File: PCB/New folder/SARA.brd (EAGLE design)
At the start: 76.2 x 76.2 mm, 46 parts, among them U1 MAX9110EKA+T, U2 MAX9110EKA+T, U3 MAX9111EKA+T, U4 MAX9111EKA+T, U5 R-78B3.3-2.0, U6 R-78B3.3-2.0

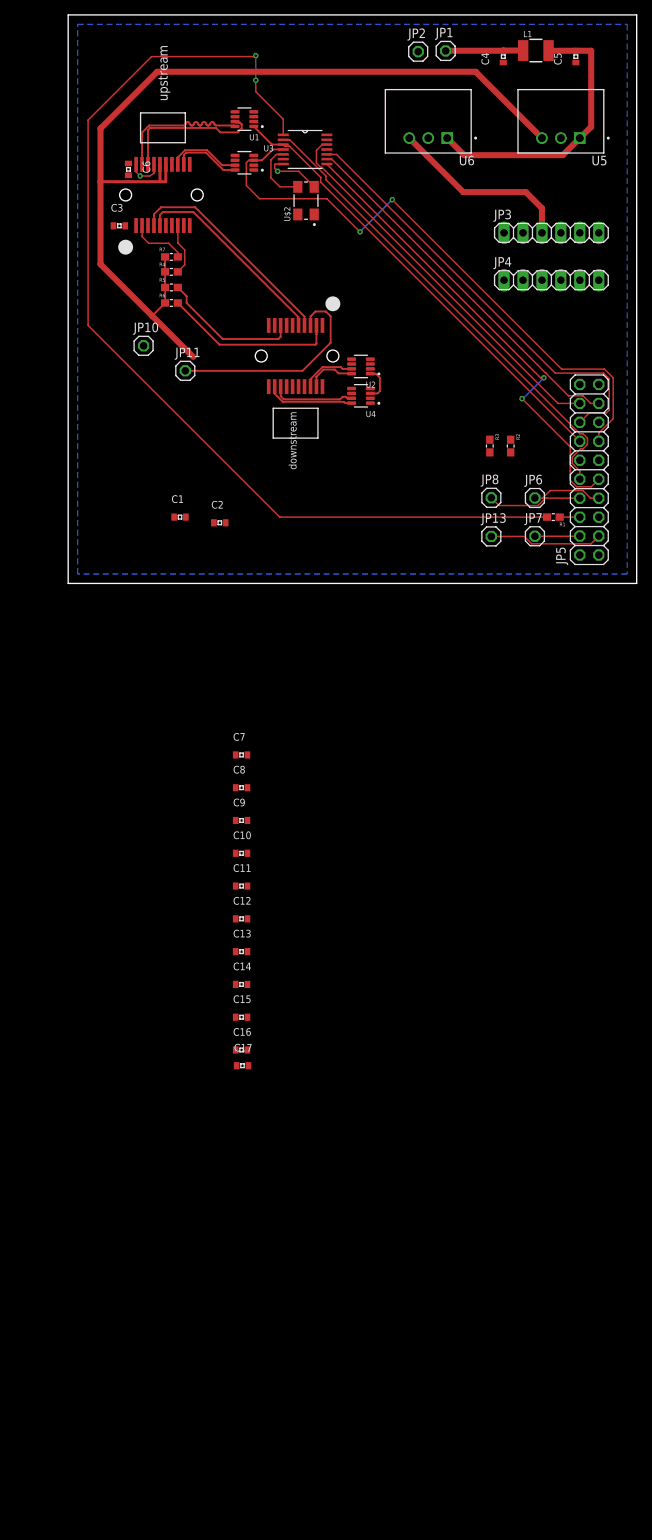
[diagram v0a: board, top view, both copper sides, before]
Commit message: 90% done routing, renamed stuff and added differental traces.
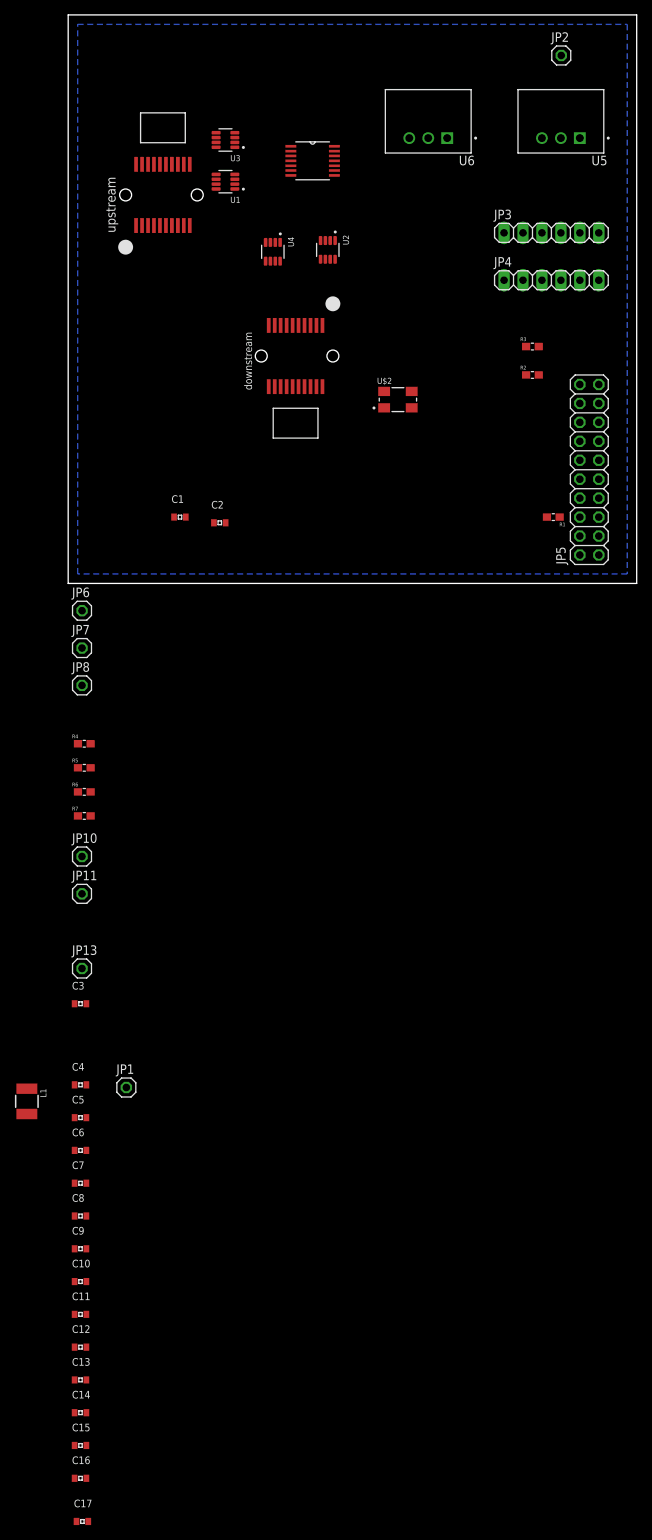
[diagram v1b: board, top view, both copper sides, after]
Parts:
- moved C5 157.0 mm to (1.65, -71.6), turned to 0 degrees
- moved L1 156.5 mm to (-5.54, -69.4), turned to 180 degrees
- moved C4 149.0 mm to (1.65, -67.2), turned to 0 degrees
- moved JP1 145.4 mm to (7.80, -67.6)
- moved C6 131.7 mm to (1.65, -76.0), turned to 0 degrees
- moved C3 104.4 mm to (1.65, -56.3)
- moved JP13 79.8 mm to (1.85, -51.6)
- moved R7 75.8 mm to (2.16, -31.2)
- moved JP11 71.5 mm to (1.85, -41.6)
- moved JP10 68.9 mm to (1.85, -36.6)
- moved R6 66.6 mm to (2.16, -27.9)
- moved R5 65.4 mm to (2.16, -24.7)
- moved C17 64.7 mm to (1.91, -125.7)
- moved R4 64.3 mm to (2.16, -21.5)
- moved JP6 62.6 mm to (1.85, -3.66)
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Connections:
- net CLOCK renamed N$6
- new net +3V1: C9.2, U1.4
- new net +3V2: C10.2, C11.2, C12.2, C13.2, C14.2, C15.2, C16.2, C17.2, R4.1, R5.1, R6.1, R7.1, SFP_DOWNSTREAM.15, SFP_DOWNSTREAM.16, SFP_UPSTREAM.15, SFP_UPSTREAM.16
- net +3V3: no longer C10.2, C11.2, C12.2, C13.2, C14.2, C15.2, C16.2, C17.2, C9.2, R4.1, R5.1, R6.1, R7.1, SFP_DOWNSTREAM.15, SFP_DOWNSTREAM.16, SFP_UPSTREAM.15, SFP_UPSTREAM.16, U1.4
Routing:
- net N$2: track 137.9 -> 0.00 mm, vias 2 -> 0
- net +3V3: track 123.8 -> 0.00 mm
- net RX_PULSE: track 81.7 -> 0.00 mm, vias 2 -> 0
- net TDC_TRIG: track 64.6 -> 0.00 mm
- net TDC_INT: track 63.3 -> 0.00 mm, vias 2 -> 0
- net TX_PULSE: track 61.6 -> 0.00 mm
- net SPI_MOSI: track 59.1 -> 0.00 mm
- net SPI_SCK: track 52.1 -> 0.00 mm
- net SPI_MISO: track 50.0 -> 0.00 mm
- net N$9: track 37.7 -> 0.00 mm
- net I2C_SDA: track 29.3 -> 0.00 mm
- net TX_DISABLE_A: track 29.0 -> 0.00 mm
- net I2C_SCL: track 27.1 -> 0.00 mm
- net +5V: track 25.0 -> 0.00 mm
- net N$20: track 23.4 -> 0.00 mm
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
